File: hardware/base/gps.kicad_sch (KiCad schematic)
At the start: 14 parts, among them U4 L96-M33

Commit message: schematic complete unreviewed
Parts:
- added Q1: Q_NMOS_DGS, Package_TO_SOT_SMD:SOT-323_SC-70, symbol Device:Q_NMOS_DGS
- D1: footprint LED_SMD:LED_0402_1005Metric -> LED_SMD:LED_0603_1608Metric
- D5: footprint LED_SMD:LED_0402_1005Metric -> LED_SMD:LED_0603_1608Metric; Label FIX -> GPS_FIX
- TP12, TP13, TP14: footprint (none) -> TestPoint:TestPoint_Pad_D1.0mm
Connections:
- net VDD_NVDC is gone; now on net VDD_AUX_3V3: C17.1, U4.8 (V_BCKP)
- net GND: now also Q1.3 (S); no longer D5.1 (K)
- net ~{RESET}: now reaches TP12.1, U4.23 (RESET)
- net GPS_FORCE_ON: now reaches TP14.1, U4.28 (FORCE_ON)
- net +3V3 renamed VDD_AUX_3V3
- net VDD_AUX_3V3: now also R28.2
- net L96_FIX renamed GPS_FIX
- net GPS_FIX: now also Q1.2 (G); no longer R28.2
- new net: D5.1 (K), Q1.1 (D)
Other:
- note removed: "Shouldn´t need reset."
- moved on the sheet: D5, R28, TP12, TP13, TP14

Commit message: placed components on board - rough
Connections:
- net VDD_AUX_3V3: no longer C17.1, U4.8 (V_BCKP)
- new net VDD_NVDC: C17.1, U4.8 (V_BCKP)
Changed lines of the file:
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@@
+    (pin "1")
+  )
+  (symbol (lib_id "bt_power:VDD_NVDC") (at 113.03 81.28 0) (unit 1)
+    (in_bom no) (on_board no)
+    (property "Reference" "#PWR0194" (id 0) (at 113.5634 81.28 0)
+      (effects (font (size 1.27 1.27)) hide)
+    )
+    (property "Value" "VDD_NVDC" (id 1) (at 113.03 77.47 0)
+      (effects (font (size 0.8 0.8)))
+    )
+    (property "Footprint" "" (id 2) (at 113.5634 81.28 0)
+      (effects (font (size 1.27 1.27)) hide)
+    )
+    (property "Datasheet" "" (id 3) (at 113.5634 81.28 0)
+      (effects (font (size 1.27 1.27)) hide)
+    )
     (pin "1")
   )
@@
       (effects (font (size 1.27 1.27)) hide)
     )
-    (pin "1")
-  )
-  (symbol (lib_id "bt_power:VDD_AUX_3V3") (at 113.03 81.28 0) (unit 1)
-    (in_bom no) (on_board no) (fields_autoplaced)
-    (property "Reference" "#PWR0194" (id 0) (at 113.5634 81.28 0)
-      (effects (font (size 1.27 1.27)) hide)
-    )
-    (property "Value" "VDD_AUX_3V3" (id 1) (at 113.03 77.47 0)
-      (effects (font (size 0.8 0.8)))
-    )
-    (property "Footprint" "" (id 2) (at 113.5634 81.28 0)
-      (effects (font (size 1.27 1.27)) hide)
-    )
-    (property "Datasheet" "" (id 3) (at 113.5634 81.28 0)
-      (effects (font (size 1.27 1.27)) hide)
-    )

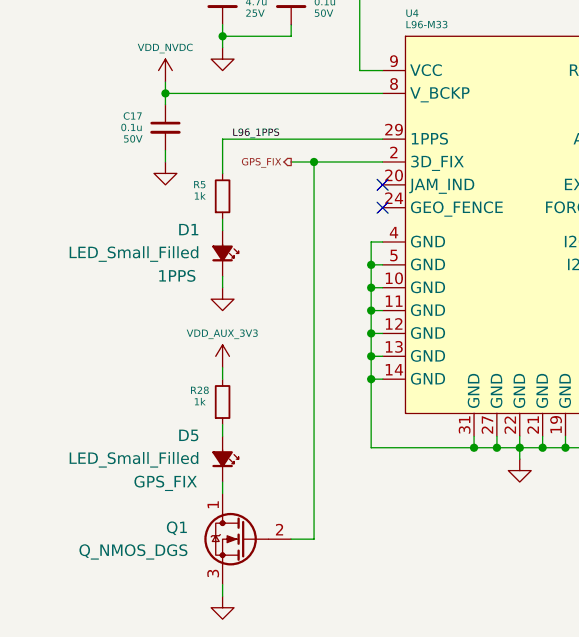
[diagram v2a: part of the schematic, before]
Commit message: Testing condensed layout
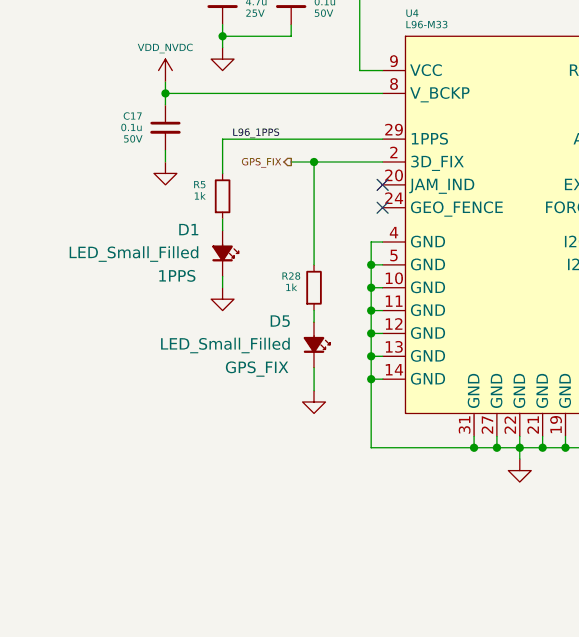
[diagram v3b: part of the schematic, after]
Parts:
- removed Q1: Q_NMOS_DGS, Package_TO_SOT_SMD:SOT-323_SC-70, symbol Device:Q_NMOS_DGS
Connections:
- net GND: now also D5.1 (K)
- net GPS_FIX: now also R28.2
- net VDD_AUX_3V3: no longer R28.2
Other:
- moved on the sheet: D5, R28
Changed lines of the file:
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@@
   (junction (at 185.42 90.17) (diameter 0) (color 0 0 0 0)
   )
+  (junction (at 129.54 90.17) (diameter 0) (color 0 0 0 0)
+  )
   (junction (at 119.38 76.2) (diameter 0) (color 0 0 0 0)
   )
@@
   )
   (junction (at 152.4 121.92) (diameter 0) (color 0 0 0 0)
-  )
-  (junction (at 129.54 90.17) (diameter 0) (color 0 0 0 0)
   )
   (junction (at 119.38 68.58) (diameter 0) (color 0 0 0 0)
@@
     (stroke (width 0) (type default) (color 0 0 0 0))
   )
+  (wire (pts (xy 129.54 90.17) (xy 137.16 90.17))
+    (stroke (width 0) (type default) (color 0 0 0 0))
+  )
   (wire (pts (xy 152.4 121.92) (xy 152.4 120.65))
     (stroke (width 0) (type default) (color 0 0 0 0))
@@
     (stroke (width 0) (type default) (color 0 0 0 0))
   )
-  (wire (pts (xy 119.38 138.43) (xy 119.38 137.16))
-    (stroke (width 0) (type default) (color 0 0 0 0))
-  )
   (wire (pts (xy 187.96 95.25) (xy 175.26 95.25))
     (stroke (width 0) (type default) (color 0 0 0 0))
@@
     (stroke (width 0) (type default) (color 0 0 0 0))
   )
-  (wire (pts (xy 119.38 113.03) (xy 119.38 114.3))
+  (wire (pts (xy 129.54 90.17) (xy 129.54 101.6))
     (stroke (width 0) (type default) (color 0 0 0 0))
   )
@@
     (stroke (width 0) (type default) (color 0 0 0 0))
   )
-  (wire (pts (xy 119.38 119.38) (xy 119.38 120.65))
+  (wire (pts (xy 129.54 106.68) (xy 129.54 107.95))
     (stroke (width 0) (type default) (color 0 0 0 0))
   )
@@
     (stroke (width 0) (type default) (color 0 0 0 0))
   )
-  (wire (pts (xy 119.38 127) (xy 119.38 125.73))
+  (wire (pts (xy 129.54 113.03) (xy 129.54 115.57))
     (stroke (width 0) (type default) (color 0 0 0 0))
   )
@@
     (stroke (width 0) (type default) (color 0 0 0 0))
   )
-  (wire (pts (xy 127 132.08) (xy 129.54 132.08))
-    (stroke (width 0) (type default) (color 0 0 0 0))
-  )
   (wire (pts (xy 194.945 80.01) (xy 194.945 76.835))
     (stroke (width 0) (type default) (color 0 0 0 0))
@@
     (stroke (width 0) (type default) (color 0 0 0 0))
   )
-  (wire (pts (xy 129.54 132.08) (xy 129.54 90.17))
-    (stroke (width 0) (type default) (color 0 0 0 0))
-  )
   (wire (pts (xy 127 74.93) (xy 127 76.2))
     (stroke (width 0) (type default) (color 0 0 0 0))
@@
   )
   (wire (pts (xy 119.38 68.58) (xy 127 68.58))
-    (stroke (width 0) (type default) (color 0 0 0 0))
-  )
-  (wire (pts (xy 129.54 90.17) (xy 137.16 90.17))
     (stroke (width 0) (type default) (color 0 0 0 0))
   )
@@
     (pin "1")
     (pin "2")
-  )
-  (symbol (lib_id "bt_power:VDD_AUX_3V3") (at 119.38 113.03 0) (unit 1)
-    (in_bom no) (on_board no) (fields_autoplaced)
-    (property "Reference" "#PWR0193" (id 0) (at 119.9134 113.03 0)
-      (effects (font (size 1.27 1.27)) hide)
-    )
-    (property "Value" "VDD_AUX_3V3" (id 1) (at 119.38 109.22 0)
-      (effects (font (size 0.8 0.8)))
-    )
-    (property "Footprint" "" (id 2) (at 119.9134 113.03 0)
-      (effects (font (size 1.27 1.27)) hide)
-    )
-    (property "Datasheet" "" (id 3) (at 119.9134 113.03 0)
-      (effects (font (size 1.27 1.27)) hide)
-    )
-    (pin "1")
   )
   (symbol (lib_id "Device:Antenna_Shield") (at 194.945 71.755 0) (unit 1)
@@
     (pin "1")
   )
-  (symbol (lib_id "Device:R_Small") (at 119.38 116.84 0) (mirror x) (unit 1)
-    (in_bom yes) (on_board yes)
-    (property "Reference" "R28" (id 0) (at 116.84 115.57 0)
-      (effects (font (size 0.8 0.8)))
-    )
-    (property "Value" "1k" (id 1) (at 116.84 116.84 0)
-      (effects (font (size 0.8 0.8)))
-    )
-    (property "Footprint" "Resistor_SMD:R_0402_1005Metric" (id 2) (at 119.38 116.84 0)
-      (effects (font (size 0.8 0.8)) hide)
-    )
-    (property "Datasheet" "~" (id 3) (at 119.38 116.84 0)
+  (symbol (lib_id "Device:R_Small") (at 129.54 104.14 0) (mirror x) (unit 1)
+    (in_bom yes) (on_board yes)
+    (property "Reference" "R28" (id 0) (at 127 102.87 0)
+      (effects (font (size 0.8 0.8)))
+    )
+    (property "Value" "1k" (id 1) (at 127 104.14 0)
+      (effects (font (size 0.8 0.8)))
+    )
+    (property "Footprint" "Resistor_SMD:R_0402_1005Metric" (id 2) (at 129.54 104.14 0)
+      (effects (font (size 0.8 0.8)) hide)
+    )
+    (property "Datasheet" "~" (id 3) (at 129.54 104.14 0)
       (effects (font (size 0.8 0.8)) hide)
     )
@@
     (pin "1")
   )
-  (symbol (lib_id "Device:LED_Small_Filled") (at 119.38 123.19 270) (mirror x) (unit 1)
-    (in_bom yes) (on_board yes)
-    (property "Reference" "D5" (id 0) (at 116.84 120.5864 90)
+  (symbol (lib_id "Device:LED_Small_Filled") (at 129.54 110.49 270) (mirror x) (unit 1)
+    (in_bom yes) (on_board yes)
+    (property "Reference" "D5" (id 0) (at 127 107.8864 90)
       (effects (font (size 1.27 1.27)) (justify right))
     )
-    (property "Value" "LED_Small_Filled" (id 1) (at 116.84 123.1264 90)
+    (property "Value" "LED_Small_Filled" (id 1) (at 127 110.4264 90)
       (effects (font (size 1.27 1.27)) (justify right))
     )
-    (property "Footprint" "LED_SMD:LED_0603_1608Metric" (id 2) (at 119.38 123.19 90)
-      (effects (font (size 1.27 1.27)) hide)
-    )
-    (property "Datasheet" "~" (id 3) (at 119.38 123.19 90)
-      (effects (font (size 1.27 1.27)) hide)
-    )
-    (property "Label" "GPS_FIX" (id 4) (at 113.03 125.73 90))
+    (property "Footprint" "LED_SMD:LED_0603_1608Metric" (id 2) (at 129.54 110.49 90)
+      (effects (font (size 1.27 1.27)) hide)
+    )
+    (property "Datasheet" "~" (id 3) (at 129.54 110.49 90)
+      (effects (font (size 1.27 1.27)) hide)
+    )
+    (property "Label" "GPS_FIX" (id 4) (at 123.19 113.03 90))
     (pin "1")
     (pin "2")
@@
     (pin "1")
   )
-  (symbol (lib_id "power:GND") (at 119.38 138.43 0) (unit 1)
+  (symbol (lib_id "power:GND") (at 129.54 115.57 0) (unit 1)
     (in_bom yes) (on_board yes) (fields_autoplaced)
-    (property "Reference" "#PWR0139" (id 0) (at 119.38 144.78 0)
-      (effects (font (size 1.27 1.27)) hide)
-    )
-    (property "Value" "GND" (id 1) (at 119.38 143.51 0)
-      (effects (font (size 1.27 1.27)) hide)
-    )
-    (property "Footprint" "" (id 2) (at 119.38 138.43 0)
-      (effects (font (size 1.27 1.27)) hide)
-    )
-    (property "Datasheet" "" (id 3) (at 119.38 138.43 0)
+    (property "Reference" "#PWR0139" (id 0) (at 129.54 121.92 0)
+      (effects (font (size 1.27 1.27)) hide)
+    )
+    (property "Value" "GND" (id 1) (at 129.54 120.65 0)
+      (effects (font (size 1.27 1.27)) hide)
+    )
+    (property "Footprint" "" (id 2) (at 129.54 115.57 0)
+      (effects (font (size 1.27 1.27)) hide)
+    )
+    (property "Datasheet" "" (id 3) (at 129.54 115.57 0)
       (effects (font (size 1.27 1.27)) hide)
     )
@@
     (pin "1")
   )
-  (symbol (lib_id "Device:Q_NMOS_DGS") (at 121.92 132.08 0) (mirror y) (unit 1)
-    (in_bom yes) (on_board yes) (fields_autoplaced)
-    (property "Reference" "Q1" (id 0) (at 115.57 130.8099 0)
-      (effects (font (size 1.27 1.27)) (justify left))
-    )
-    (property "Value" "Q_NMOS_DGS" (id 1) (at 115.57 133.3499 0)
-      (effects (font (size 1.27 1.27)) (justify left))
-    )
-    (property "Footprint" "Package_TO_SOT_SMD:SOT-323_SC-70" (id 2) (at 116.84 129.54 0)
-      (effects (font (size 1.27 1.27)) hide)
-    )
-    (property "Datasheet" "~" (id 3) (at 121.92 132.08 0)
-      (effects (font (size 1.27 1.27)) hide)
-    )
-    (pin "1")
-    (pin "2")
-    (pin "3")
-  )
   (symbol (lib_id "Device:R_Small") (at 179.07 80.01 270) (unit 1)

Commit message: layout
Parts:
- removed TP12: GPS_RST, TestPoint:TestPoint_Pad_D1.0mm, symbol Connector:TestPoint
- removed TP13: GPS_INT, TestPoint:TestPoint_Pad_D1.0mm, symbol Connector:TestPoint
- added TP1: GPS_FON, TestPoint:TestPoint_Pad_D1.0mm, symbol Connector:TestPoint
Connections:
- net GPS_EXTINT0: now reaches U4.7 (EXTINT0)
- net GPS_EXTINT0: now also TP1.1
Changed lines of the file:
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@@
   (junction (at 154.94 121.92) (diameter 0) (color 0 0 0 0)
-  )
-  (junction (at 185.42 90.17) (diameter 0) (color 0 0 0 0)
   )
   (junction (at 129.54 90.17) (diameter 0) (color 0 0 0 0)
@@
     (stroke (width 0) (type default) (color 0 0 0 0))
   )
+  (wire (pts (xy 167.64 92.71) (xy 179.07 92.71))
+    (stroke (width 0) (type default) (color 0 0 0 0))
+  )
   (wire (pts (xy 147.32 121.92) (xy 149.86 121.92))
     (stroke (width 0) (type default) (color 0 0 0 0))
@@
     (stroke (width 0) (type default) (color 0 0 0 0))
   )
-  (wire (pts (xy 167.64 90.17) (xy 185.42 90.17))
+  (wire (pts (xy 167.64 90.17) (xy 187.96 90.17))
     (stroke (width 0) (type default) (color 0 0 0 0))
   )
@@
     (stroke (width 0) (type default) (color 0 0 0 0))
   )
-  (wire (pts (xy 185.42 96.52) (xy 185.42 90.17))
-    (stroke (width 0) (type default) (color 0 0 0 0))
-  )
   (wire (pts (xy 127 69.85) (xy 127 68.58))
     (stroke (width 0) (type default) (color 0 0 0 0))
@@
     (stroke (width 0) (type default) (color 0 0 0 0))
   )
+  (wire (pts (xy 179.07 96.52) (xy 179.07 92.71))
+    (stroke (width 0) (type default) (color 0 0 0 0))
+  )
   (bus (pts (xy 207.01 100.33) (xy 209.55 100.33))
     (stroke (width 0) (type default) (color 0 0 0 0))
@@
     (stroke (width 0) (type default) (color 0 0 0 0))
   )
-  (wire (pts (xy 187.96 90.17) (xy 185.42 90.17))
-    (stroke (width 0) (type default) (color 0 0 0 0))
-  )
   (wire (pts (xy 149.86 121.92) (xy 149.86 120.65))
     (stroke (width 0) (type default) (color 0 0 0 0))
@@
     (stroke (width 0) (type default) (color 0 0 0 0))
   )
-  (wire (pts (xy 180.34 92.71) (xy 180.34 96.52))
-    (stroke (width 0) (type default) (color 0 0 0 0))
-  )
   (wire (pts (xy 149.86 121.92) (xy 152.4 121.92))
     (stroke (width 0) (type default) (color 0 0 0 0))
@@
   )
   (wire (pts (xy 167.64 105.41) (xy 203.2 105.41))
-    (stroke (width 0) (type default) (color 0 0 0 0))
-  )
-  (wire (pts (xy 167.64 92.71) (xy 180.34 92.71))
     (stroke (width 0) (type default) (color 0 0 0 0))
   )
@@
     (at 200.66 96.52 0)
     (effects (font (size 0.8 0.8)) (justify left bottom))
+  )
+  (label "GPS_EXTINT0" (at 179.07 92.71 180)
+    (effects (font (size 0.8 0.8)) (justify right bottom))
   )
   (label "ANT_RF" (at 189.865 80.01 0)
@@
     (pin "2")
   )
-  (symbol (lib_id "Connector:TestPoint") (at 185.42 96.52 180) (unit 1)
-    (in_bom yes) (on_board yes)
-    (property "Reference" "TP12" (id 0) (at 185.42 102.87 0)
-      (effects (font (size 0.8 0.8)))
-    )
-    (property "Value" "GPS_RST" (id 1) (at 185.42 105.41 90)
-      (effects (font (size 1.27 1.27)) hide)
-    )
-    (property "Footprint" "TestPoint:TestPoint_Pad_D1.0mm" (id 2) (at 180.34 96.52 0)
-      (effects (font (size 1.27 1.27)) hide)
-    )
-    (property "Datasheet" "~" (id 3) (at 180.34 96.52 0)
-      (effects (font (size 1.27 1.27)) hide)
-    )
-    (pin "1")
-  )
   (symbol (lib_id "Device:R_Small") (at 129.54 104.14 0) (mirror x) (unit 1)
     (in_bom yes) (on_board yes)
@@
     (pin "1")
     (pin "2")
-  )
-  (symbol (lib_id "Connector:TestPoint") (at 180.34 96.52 180) (unit 1)
-    (in_bom yes) (on_board yes)
-    (property "Reference" "TP13" (id 0) (at 180.34 102.87 0)
-      (effects (font (size 0.8 0.8)))
-    )
-    (property "Value" "GPS_INT" (id 1) (at 180.34 105.41 90)
-      (effects (font (size 1.27 1.27)) hide)
-    )
-    (property "Footprint" "TestPoint:TestPoint_Pad_D1.0mm" (id 2) (at 175.26 96.52 0)
-      (effects (font (size 1.27 1.27)) hide)
-    )
-    (property "Datasheet" "~" (id 3) (at 175.26 96.52 0)
-      (effects (font (size 1.27 1.27)) hide)
-    )
-    (pin "1")
   )
   (symbol (lib_id "power:GND") (at 119.38 77.47 0) (unit 1)
@@
     (pin "2")
   )
+  (symbol (lib_id "Connector:TestPoint") (at 179.07 96.52 180) (unit 1)
+    (in_bom yes) (on_board yes)
+    (property "Reference" "TP1" (id 0) (at 179.07 102.87 0)
+      (effects (font (size 0.8 0.8)))
+    )
+    (property "Value" "GPS_FON" (id 1) (at 179.07 105.41 90)
+      (effects (font (size 1.27 1.27)) hide)
+    )
+    (property "Footprint" "TestPoint:TestPoint_Pad_D1.0mm" (id 2) (at 173.99 96.52 0)
+      (effects (font (size 1.27 1.27)) hide)
+    )
+    (property "Datasheet" "~" (id 3) (at 173.99 96.52 0)
+      (effects (font (size 1.27 1.27)) hide)
+    )
+    (pin "1")
+  )
   (symbol (lib_id "Device:R_Small") (at 119.38 93.98 0) (mirror x) (unit 1)

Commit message: more layout, optimising i2c
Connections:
- net 1pps_led: now reaches D1.2 (A), R5.1
- net 3df_led: now reaches D5.2 (A), R28.1
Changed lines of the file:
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@@
+    (effects (font (size 0.8 0.8)) (justify left bottom))
+  )
+  (label "1pps_led" (at 119.38 97.79 0)
     (effects (font (size 0.8 0.8)) (justify left bottom))
   )
@@
     (effects (font (size 0.8 0.8)) (justify right bottom))
   )
+  (label "3df_led" (at 129.54 107.95 0)
+    (effects (font (size 0.8 0.8)) (justify left bottom))
+  )
   (label "GPS_UART.RX" (at 203.2 105.41 180)

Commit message: Tidied up, added more stitches
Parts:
- added TP2: GPS_FON, TestPoint:TestPoint_Pad_D1.0mm, symbol Connector:TestPoint
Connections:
- net ~{RESET} renamed GPS_RESET
- net GPS_RESET: now also TP2.1
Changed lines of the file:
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@@
+    (stroke (width 0) (type default) (color 0 0 0 0))
+  )
+  (wire (pts (xy 182.88 96.52) (xy 182.88 90.17))
     (stroke (width 0) (type default) (color 0 0 0 0))
   )
@@
     (stroke (width 0) (type default) (color 0 0 0 0))
   )
-  (wire (pts (xy 167.64 90.17) (xy 187.96 90.17))
+  (wire (pts (xy 167.64 90.17) (xy 182.88 90.17))
     (stroke (width 0) (type default) (color 0 0 0 0))
   )
@@
     (effects (font (size 0.8 0.8)) (justify left bottom))
   )
-  (global_label "~{RESET}" (shape input) (at 187.96 90.17 0) (fields_autoplaced)
-    (effects (font (size 0.8 0.8)) (justify left))
-    (property "Intersheet References" "${INTERSHEET_REFS}" (id 0) (at 193.099 90.12 0)
-      (effects (font (size 0.8 0.8)) (justify left))
-    )
+  (label "GPS_RESET" (at 182.88 90.17 180)
+    (effects (font (size 0.8 0.8)) (justify right bottom))
   )
   (hierarchical_label "GPS_FIX" (shape output) (at 127 90.17 180)
@@
       (effects (font (size 1.27 1.27)) hide)
     )
+    (pin "1")
+  )
+  (symbol (lib_id "Connector:TestPoint") (at 182.88 96.52 180) (unit 1)
+    (in_bom yes) (on_board yes)
+    (property "Reference" "TP2" (id 0) (at 182.88 102.87 0)
+      (effects (font (size 0.8 0.8)))
+    )
+    (property "Value" "GPS_FON" (id 1) (at 182.88 105.41 90)
+      (effects (font (size 1.27 1.27)) hide)
+    )
+    (property "Footprint" "TestPoint:TestPoint_Pad_D1.0mm" (id 2) (at 177.8 96.52 0)
+      (effects (font (size 1.27 1.27)) hide)
+    )
+    (property "Datasheet" "~" (id 3) (at 177.8 96.52 0)
+      (effects (font (size 1.27 1.27)) hide)
+    )
